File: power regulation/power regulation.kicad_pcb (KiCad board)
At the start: 4 copper layers, 175 x 100 mm, 95 parts, among them J1 Conn_01x02_Pin, J2 Conn_01x02_Pin, J3 Conn_01x02_Pin, M1 TO-236AB_SOT23_NEX, M2 TO-236AB_SOT23_NEX, U1 LT8640SEV_PBF, U2 LT8640SEV_PBF, U3 LT8619EDD-TRPBF, U4 LAA108STR, U5 SOP65P640X110-14N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

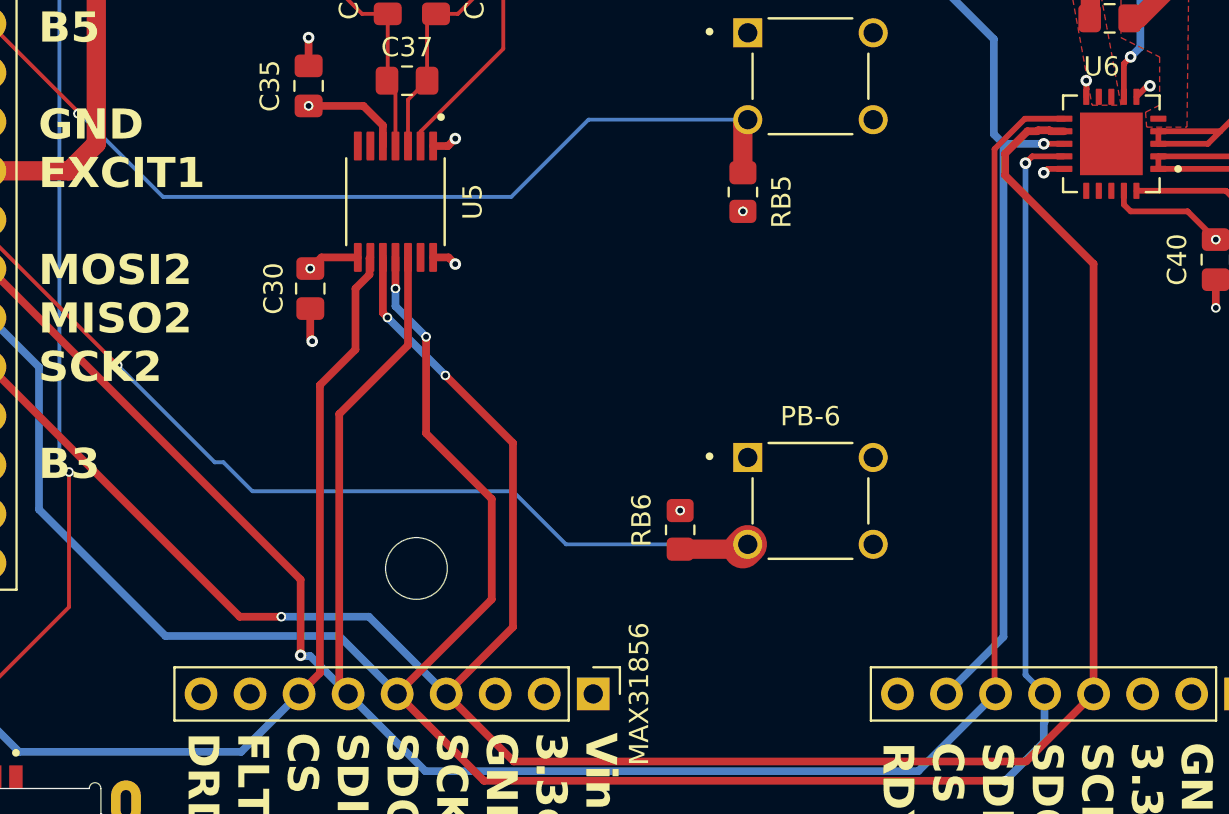
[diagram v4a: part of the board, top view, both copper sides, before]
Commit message: Connect drdy pins of max module to headers.
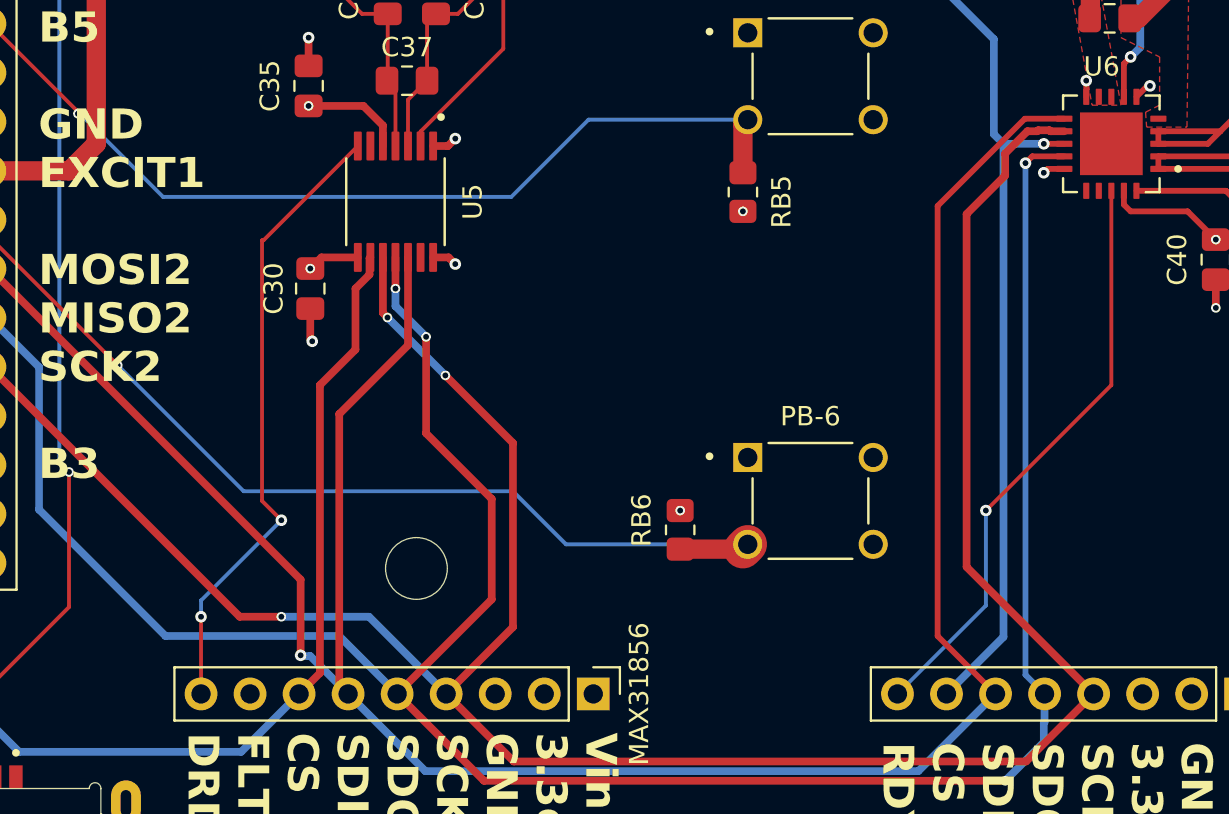
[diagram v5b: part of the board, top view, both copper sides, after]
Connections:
- MAX31856 pad 9: (no net) -> thermDRDY
- MAX31865 pad 8: (no net) -> RTDDRDY
- U5 pad 7: (no net) -> thermDRDY
- U6 pad 18: (no net) -> RTDDRDY
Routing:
- net thermDRDY: track 0.00 -> 32.6 mm, vias 0 -> 2
- net RTDDRDY: track 0.00 -> 30.7 mm, vias 0 -> 1
- net MAX_SDI: track 123.6 -> 126.1 mm
- net MAX_SCK: track 127.4 -> 129.1 mm
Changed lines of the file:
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@@
 	(net 78 "SD_CS")
 	(net 79 "HeaterPre")
+	(net 80 "thermDRDY")
+	(net 81 "RTDDRDY")
 	(footprint "Connector_PinHeader_2.54mm:PinHeader_2x19_P2.54mm_Vertical"
 		(layer "F.Cu")
@@
 			(layers "*.Cu" "*.Mask")
 			(remove_unused_layers no)
+			(net 80 "thermDRDY")
 		)
 		(embedded_fonts no)
@@
 			(layers "F.Cu" "F.Mask" "F.Paste")
 			(roundrect_rratio 0.125)
+			(net 81 "RTDDRDY")
 			(solder_mask_margin 0.102)
 		)
@@
 			(layers "*.Cu" "*.Mask")
 			(remove_unused_layers no)
+			(net 81 "RTDDRDY")
 		)
 		(embedded_fonts no)
@@
 			(layers "F.Cu" "F.Mask" "F.Paste")
 			(roundrect_rratio 0.125)
+			(net 80 "thermDRDY")
 			(solder_mask_margin 0.102)
 		)
@@
 	)
 	(segment
-		(start 219 93)
-		(end 219 94.14)
+		(start 179.3425 117)
+		(end 166.4025 104.06)
 		(width 0.4)
 		(layer "F.Cu")
@@
 	)
 	(segment
-		(start 223.58 98.72)
-		(end 223.58 121)
+		(start 220.15 91.85)
+		(end 219 93)
 		(width 0.4)
 		(layer "F.Cu")
@@
 	)
 	(segment
-		(start 179.3425 117)
-		(end 166.4025 104.06)
+		(start 220.709636 91.799)
+		(end 220.658636 91.85)
+		(width 0.4)
+		(layer "F.Cu")
+		(net 44)
+	)
+	(segment
+		(start 219 94.14)
+		(end 217 96.14)
 		(width 0.4)
 		(layer "F.Cu")
@@
 	)
 	(segment
-		(start 187 101.5)
-		(end 186.7625 101.2625)
+		(start 222.065 91.85)
+		(end 221.341364 91.85)
 		(width 0.4)
 		(layer "F.Cu")
@@
 	)
 	(segment
-		(start 220.709636 91.799)
-		(end 220.658636 91.85)
+		(start 221.290364 91.799)
+		(end 220.709636 91.799)
 		(width 0.4)
 		(layer "F.Cu")
@@
 	)
 	(segment
-		(start 193.5 117.54)
-		(end 193.5 108)
+		(start 187 101.5)
+		(end 186.7625 101.2625)
 		(width 0.4)
 		(layer "F.Cu")
@@
 	)
 	(segment
-		(start 193.5 108)
-		(end 190 104.5)
+		(start 193.5 117.54)
+		(end 193.5 108)
 		(width 0.4)
 		(layer "F.Cu")
@@
 	)
 	(segment
-		(start 181.5 117)
-		(end 179.3425 117)
+		(start 221.341364 91.85)
+		(end 221.290364 91.799)
 		(width 0.4)
 		(layer "F.Cu")
@@
 	)
 	(segment
-		(start 193.54 124.5)
-		(end 220.08 124.5)
+		(start 217 114.42)
+		(end 223.58 121)
 		(width 0.4)
 		(layer "F.Cu")
@@
 	)
 	(segment
-		(start 190.04 121)
-		(end 193.54 124.5)
+		(start 193.5 108)
+		(end 190 104.5)
 		(width 0.4)
 		(layer "F.Cu")
@@
 	)
 	(segment
-		(start 222.065 91.85)
-		(end 221.341364 91.85)
+		(start 220.658636 91.85)
+		(end 220.15 91.85)
 		(width 0.4)
 		(layer "F.Cu")
@@
 	)
 	(segment
-		(start 219 94.14)
-		(end 223.58 98.72)
+		(start 181.5 117)
+		(end 179.3425 117)
 		(width 0.4)
 		(layer "F.Cu")
@@
 	)
 	(segment
-		(start 220.08 124.5)
-		(end 223.58 121)
+		(start 219 93)
+		(end 219 94.14)
 		(width 0.4)
 		(layer "F.Cu")
@@
 	)
 	(segment
-		(start 221.290364 91.799)
-		(end 220.709636 91.799)
+		(start 193.54 124.5)
+		(end 220.08 124.5)
 		(width 0.4)
 		(layer "F.Cu")
@@
 	)
 	(segment
-		(start 221.341364 91.85)
-		(end 221.290364 91.799)
+		(start 190.04 121)
+		(end 193.54 124.5)
 		(width 0.4)
 		(layer "F.Cu")
@@
 	)
 	(segment
-		(start 220.15 91.85)
-		(end 219 93)
+		(start 217 96.14)
+		(end 217 114.42)
 		(width 0.4)
 		(layer "F.Cu")
@@
 	)
 	(segment
-		(start 186.7625 101.2625)
-		(end 186.7625 98.385)
+		(start 220.08 124.5)
+		(end 223.58 121)
 		(width 0.4)
 		(layer "F.Cu")
@@
 	)
 	(segment
-		(start 220.658636 91.85)
-		(end 220.15 91.85)
+		(start 186.7625 101.2625)
+		(end 186.7625 98.385)
 		(width 0.4)
 		(layer "F.Cu")
@@
 	)
 	(segment
-		(start 218.449 120.949)
-		(end 218.5 121)
-		(width 0.3)
+		(start 184.96 121)
+		(end 184.5 120.54)
+		(width 0.4)
 		(layer "F.Cu")
 		(net 46)
 	)
 	(segment
-		(start 184.96 121)
-		(end 184.5 120.54)
-		(width 0.4)
+		(start 215.5 118)
+		(end 218.5 121)
+		(width 0.3)
 		(layer "F.Cu")
 		(net 46)
@@
 	)
 	(segment
-		(start 218.449 92.771768)
-		(end 218.449 120.949)
-		(width 0.3)
+		(start 182.5 119)
+		(end 182.5 115.0775)
+		(width 0.4)
 		(layer "F.Cu")
 		(net 46)
@@
 	)
 	(segment
-		(start 182.5 119)
-		(end 182.5 115.0775)
-		(width 0.4)
-		(layer "F.Cu")
-		(net 46)
-	)
-	(segment
 		(start 184.5 106.5)
 		(end 188.0625 102.9375)
@@
 	(segment
 		(start 220.020768 91.2)
-		(end 218.449 92.771768)
+		(end 215.5 95.720768)
+		(width 0.3)
+		(layer "F.Cu")
+		(net 46)
+	)
+	(segment
+		(start 215.5 95.720768)
+		(end 215.5 118)
 		(width 0.3)
 		(layer "F.Cu")
@@
 	)
 	(segment
-		(start 178.5 109)
-		(end 180 110.5)
-		(width 0.2)
-		(layer "B.Cu")
-		(net 73)
-	)
-	(segment
 		(start 173.02513 103.97487)
-		(end 178.05026 109)
+		(end 179.55026 110.5)
 		(width 0.2)
 		(layer "B.Cu")
@@
 	)
 	(segment
-		(start 178.05026 109)
-		(end 178.5 109)
+		(start 193.5 110.5)
+		(end 196.25 113.25)
 		(width 0.2)
 		(layer "B.Cu")
@@
 	)
 	(segment
-		(start 180 110.5)
+		(start 179.55026 110.5)
 		(end 193.5 110.5)
 		(width 0.2)
@@
 	)
 	(segment
-		(start 193.5 110.5)
-		(end 196.25 113.25)
-		(width 0.2)
-		(layer "B.Cu")
-		(net 73)
-	)
-	(segment
 		(start 156.5025 116.5)
 		(end 163.8625 109.14)
@@
 		(net 79)
 	)
+	(segment
+		(start 180.5 111)
+		(end 181.5 112)
+		(width 0.2)
+		(layer "F.Cu")
+		(net 80)
+	)
+	(segment
+		(start 180.5 97.5)
+		(end 180.5 111)
+		(width 0.2)
+		(layer "F.Cu")
+		(net 80)
+	)
+	(segment
+		(start 177.34 117)
+		(end 177.34 121)
+		(width 0.2)
+		(layer "F.Cu")
+		(net 80)
+	)
+	(segment
+		(start 185.4625 92.615)
+		(end 180.5775 97.5)
+		(width 0.2)
+		(layer "F.Cu")
+		(net 80)
+	)
+	(segment
+		(start 180.5775 97.5)
+		(end 180.5 97.5)
+		(width 0.2)
+		(layer "F.Cu")
+		(net 80)
+	)
+	(via
+		(at 177.34 117)
+		(size 0.6)
+		(drill 0.3)
+		(layers "F.Cu" "B.Cu")
+		(net 80)
+	)
+	(via
+		(at 181.5 112)
+		(size 0.6)
+		(drill 0.3)
+		(layers "F.Cu" "B.Cu")
+		(net 80)
+	)
+	(segment
+		(start 177.34 117)
+		(end 177.34 116.16)
+		(width 0.2)
+		(layer "B.Cu")
+		(net 80)
+	)
+	(segment
+		(start 177.34 116.16)
+		(end 181.5 112)
+		(width 0.2)
+		(layer "B.Cu")
+		(net 80)
+	)
+	(segment
+		(start 218 111.5)
+		(end 224.5 105)
+		(width 0.2)
+		(layer "F.Cu")
+		(net 81)
+	)
+	(segment
+		(start 224.5 105)
+		(end 224.5 94.935)
+		(width 0.2)
+		(layer "F.Cu")
+		(net 81)
+	)
+	(via
+		(at 218 111.5)
+		(size 0.6)
+		(drill 0.3)
+		(layers "F.Cu" "B.Cu")
+		(net 81)
+	)
+	(segment
+		(start 218 116.42)
+		(end 218 111.5)
+		(width 0.2)
+		(layer "B.Cu")
+		(net 81)
+	)
+	(segment
+		(start 213.42 121)
+		(end 218 116.42)
+		(width 0.2)
+		(layer "B.Cu")
+		(net 81)
+	)
 	(zone
 		(net 53)
@@
 		)
 	)
-	(group ""
-		(members "076e5f9d-cd1b-4b00-8654-8aeae8b3cde5" "18b88f51-d585-47b6-a430-fb65247ba183"
-			"1a234fb7-730c-4ffd-bad0-6650092479f4" "2bb28341-098e-4fd6-b1e0-a07fe559ec97"
-			"306b052e-59c2-48a8-9fed-05438348ce43" "36d1a53e-a1ad-4420-8dee-7418a9bcba4f"
-			"46973877-2da3-4a2a-bdf3-5e73dcd17ff0" "4934616f-5e6b-487c-b708-aa456d4e4309"
-			"5900354d-4e2e-4156-9267-451853dc1430" "62ef15cd-1ba8-473d-a965-feef60ab2fe0"
-			"708e637f-d6da-4249-96fb-6ae9e31dcd74" "71f4891c-d5bd-4e04-83a4-bc0e15a9d176"
-			"75134314-6b59-40ce-a976-23387675d6c9" "7ac86e22-3009-48d2-9b5d-a77885b1e944"
-			"7be709ea-2137-4edb-bee7-344cd5830129" "813785b8-ccde-4444-953c-dcb41b735eb2"
-			"9b06d370-e002-4503-bfd9-fa243027f2ea" "a3529c68-b31b-4528-ad73-e3ab057e0326"
-			"b344efee-6110-4002-a2d6-6f41df3ebbfd" "d4259343-b2d7-4acd-bd66-75caa03fcb93"
-			"e1b3202a-3491-4721-b030-dc6bbd22a74e" "f3c1c028-282a-4423-9483-963a842c32fe"
-			"f72d6468-3363-4269-a405-e1081a09338b" "fb36552c-5949-4db2-b917-ff8b26e8ac9f"
-			"fbbe9dd7-3516-4ac1-92bc-6865fd94144f"
-		)
-	)

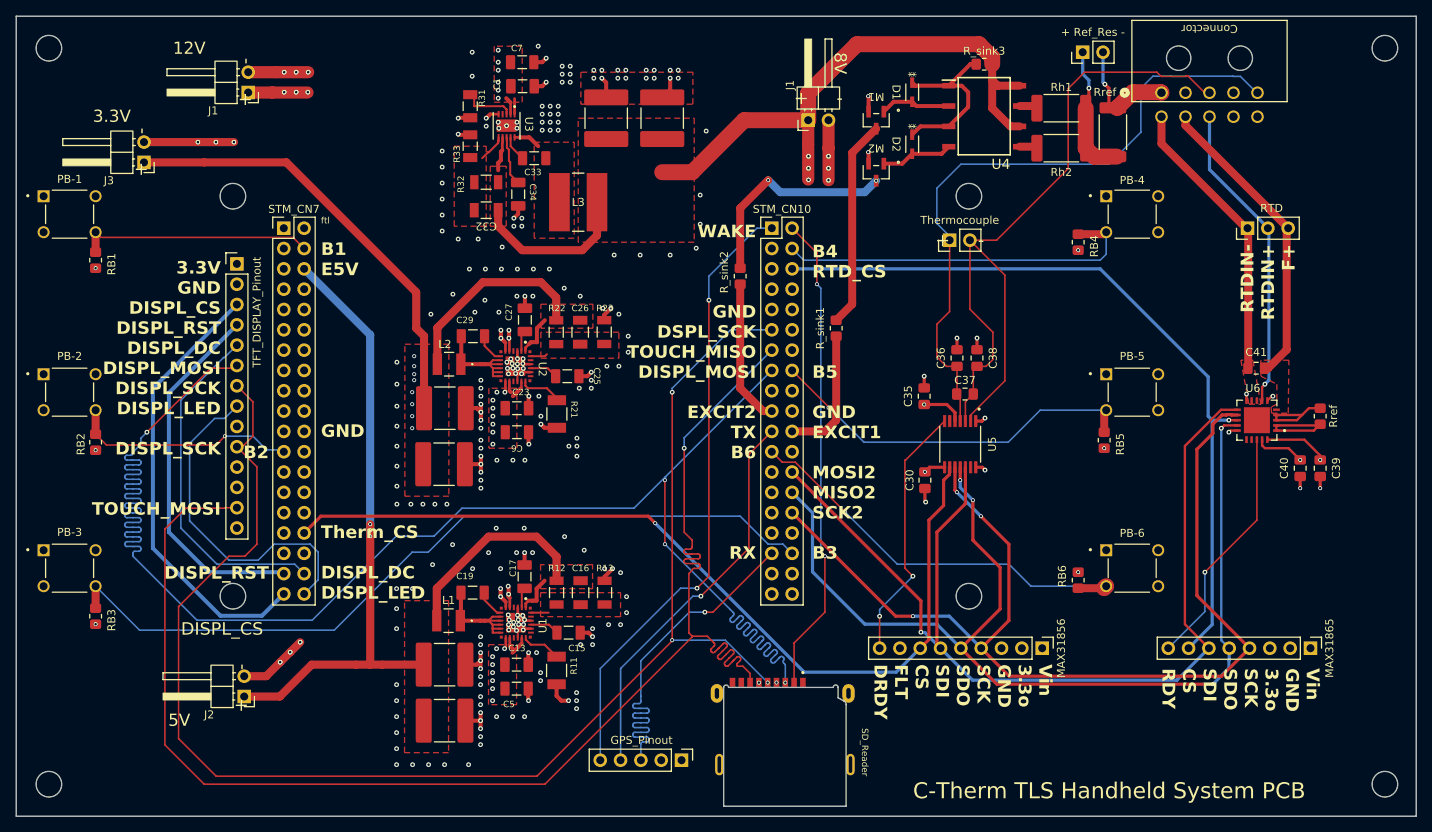
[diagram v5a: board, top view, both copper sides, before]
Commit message: Space out vias for non power planes and thicken power header traces.
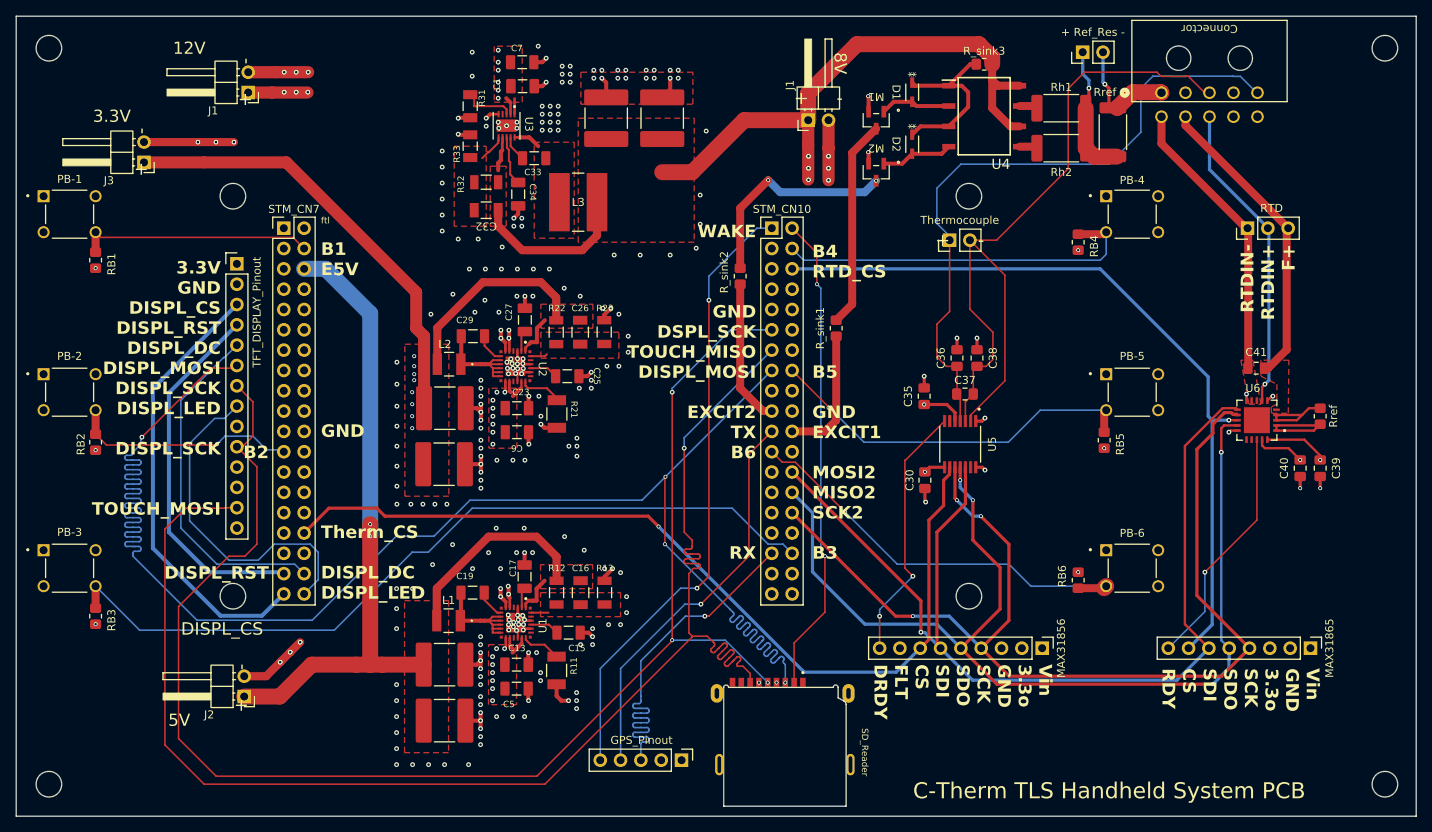
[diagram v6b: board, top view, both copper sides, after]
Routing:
- net /5V: track 109.1 -> 110.7 mm
- net Therm_CS: track 111.4 -> 112.2 mm
- net B3: track 99.9 -> 100.7 mm
- net MAX_SCK: track 129.1 -> 129.9 mm
- net TX: track 49.5 -> 50.1 mm

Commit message: Add marc's changes to the power reg ccts.
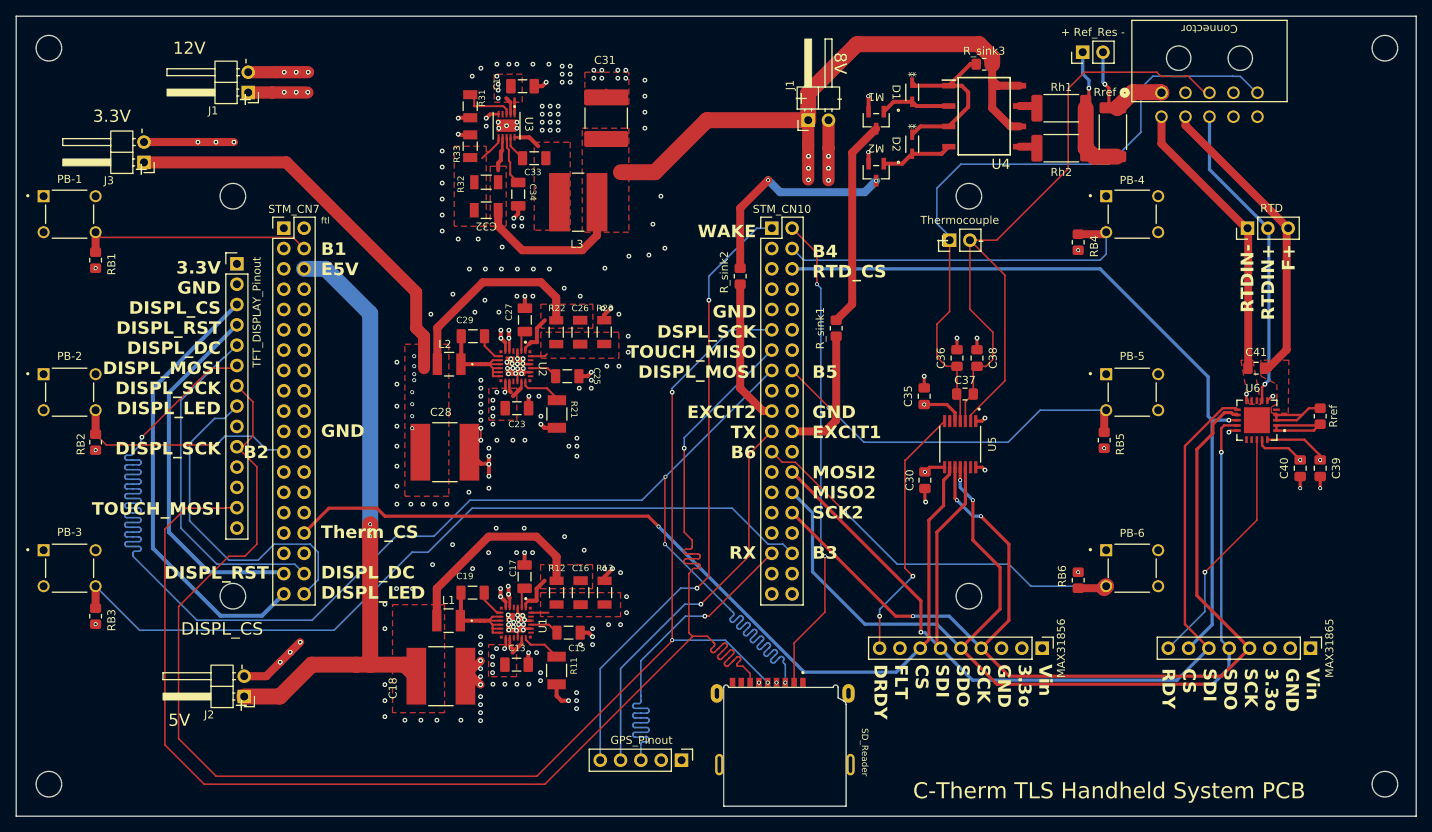
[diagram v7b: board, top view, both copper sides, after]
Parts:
- removed C2, C3, C4: 22uF, KRM55QR71H226KH13K:CAPC6153X390N
- removed C5, C6, C7: 0.1uF, CL31B104KBCNNNC:CAPC3216X100N
- C13, C23: value 4.7uF -> 1uF
- C18, C28: value 22uF -> 100uF; footprint KRM55QR71H226KH13K:CAPC6153X390N -> footprints00:CAP_NTJ_76B_9.5T_NIP
- moved C28 5.50 mm to (123.0, 96.5)
- moved C18 1.51 mm to (122.5, 124.5)
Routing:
- net GND: track 116.5 -> 105.2 mm, vias 250 -> 241
- net /8V: track 98.7 -> 103.9 mm
- net /3.3V: track 108.6 -> 103.6 mm
- net /Pin: vias 33 -> 26
